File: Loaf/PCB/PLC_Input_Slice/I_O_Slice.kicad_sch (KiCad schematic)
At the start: 23 parts, among them J1 Screw_Terminal_01x02, J10 Screw_Terminal_01x02, J11 Screw_Terminal_01x02, J12 Screw_Terminal_01x02, J13 Screw_Terminal_01x02, J14 Screw_Terminal_01x02, J15 Screw_Terminal_01x02, J16 Screw_Terminal_01x02, J2 Screw_Terminal_01x02, J3 Screw_Terminal_01x02, J4 Screw_Terminal_01x02, J5 Screw_Terminal_01x02, J6 Screw_Terminal_01x02, J7 Screw_Terminal_01x02, J8 Screw_Terminal_01x02, J9 Screw_Terminal_01x02, U1 MCP4922-EP, U2 MCP4922-EP, U3 MCP4922-EP, U4 MCP4922-EP, U5 MCP3208

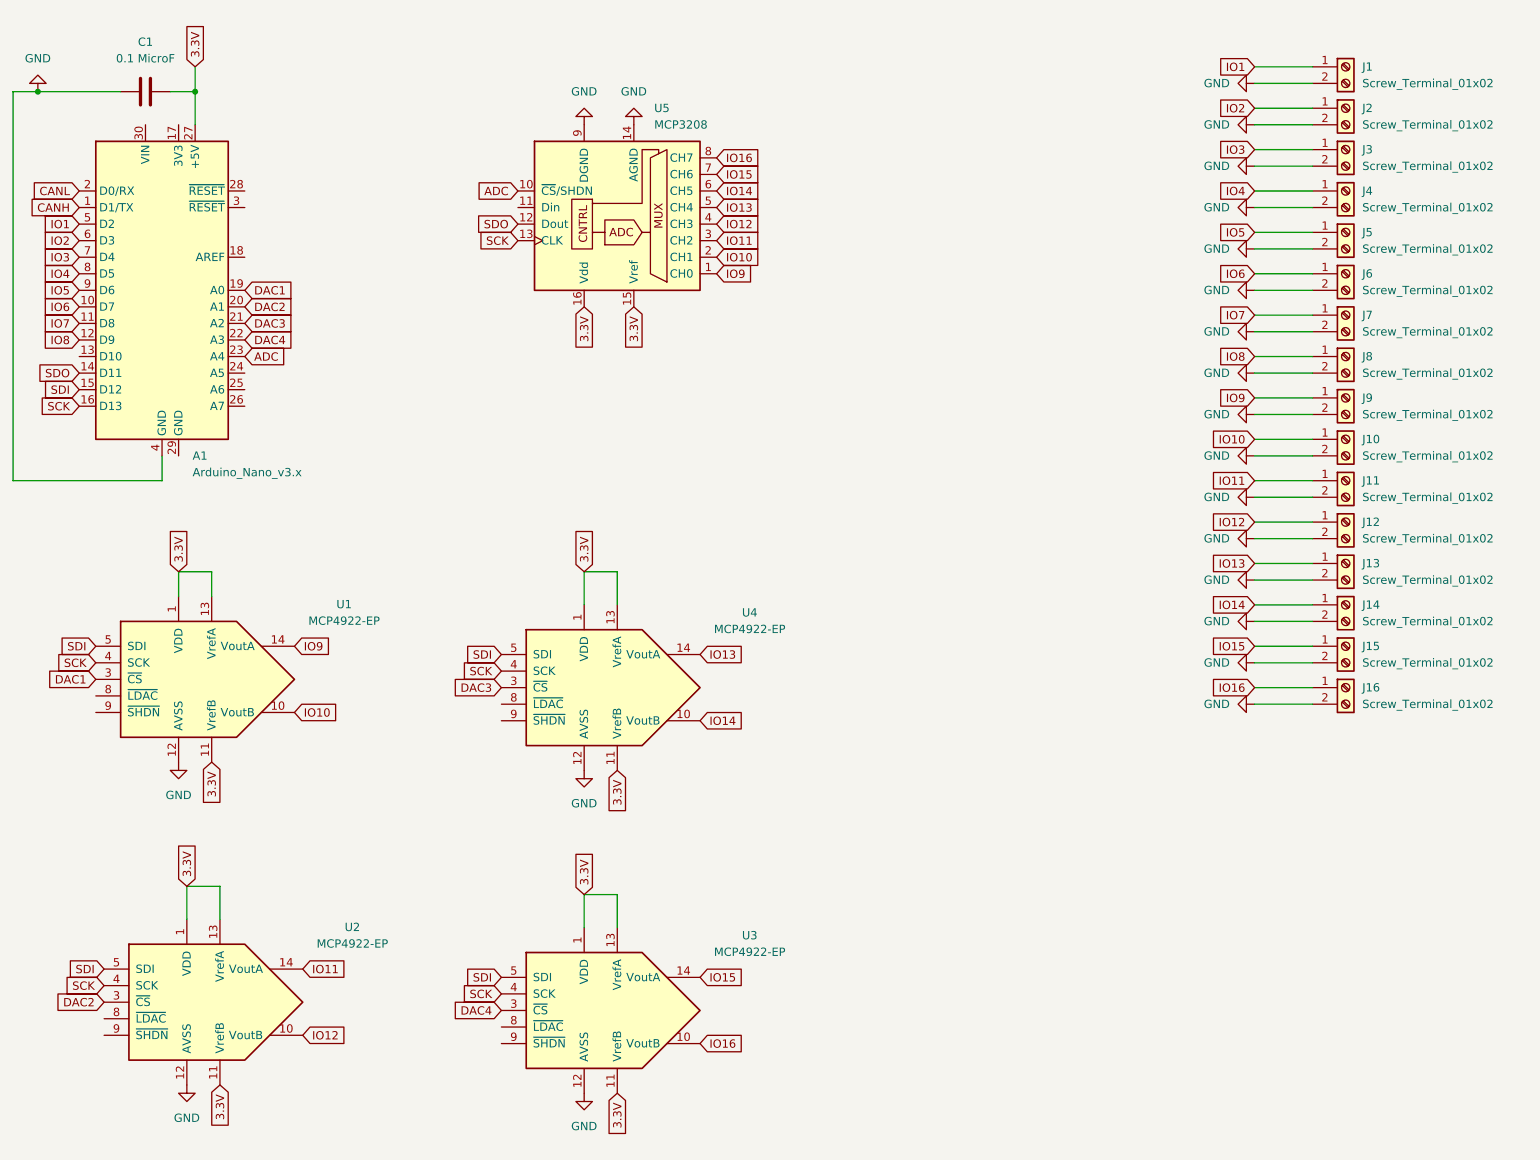
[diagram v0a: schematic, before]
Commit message: Updated IO slice schematic
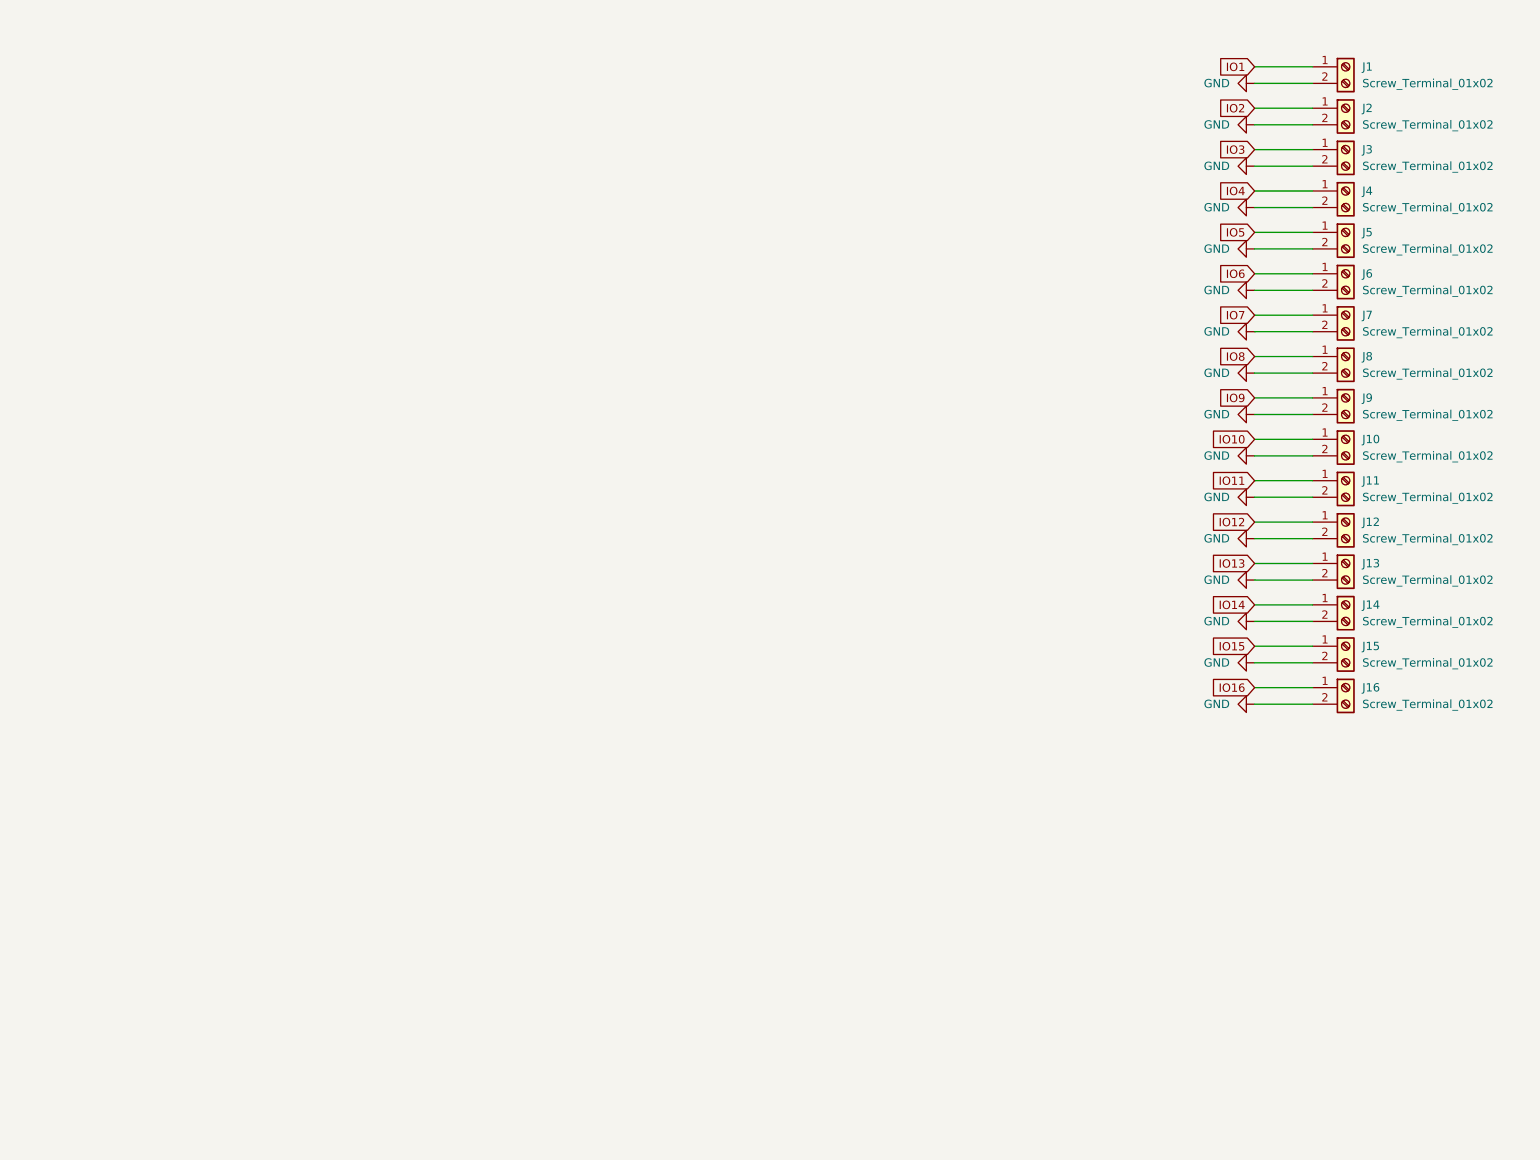
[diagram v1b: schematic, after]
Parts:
- removed A1: Arduino_Nano_v3.x, Module:Arduino_Nano, symbol MCU_Module:Arduino_Nano_v3.x
- removed C1: 0.1 MicroF, Capacitor_THT:C_Disc_D10.0mm_W2.5mm_P5.00mm, symbol Device:C
- removed U1, U2, U3, U4: MCP4922-EP, Package_DIP:DIP-14_W10.16mm_LongPads, symbol Analog_DAC:MCP4922-EP
- removed U5: MCP3208, Package_DIP:DIP-16_W7.62mm_LongPads, symbol Analog_ADC:MCP3208
